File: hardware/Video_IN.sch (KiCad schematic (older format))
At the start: 2 parts, among them U4 DS90CF363AMTD

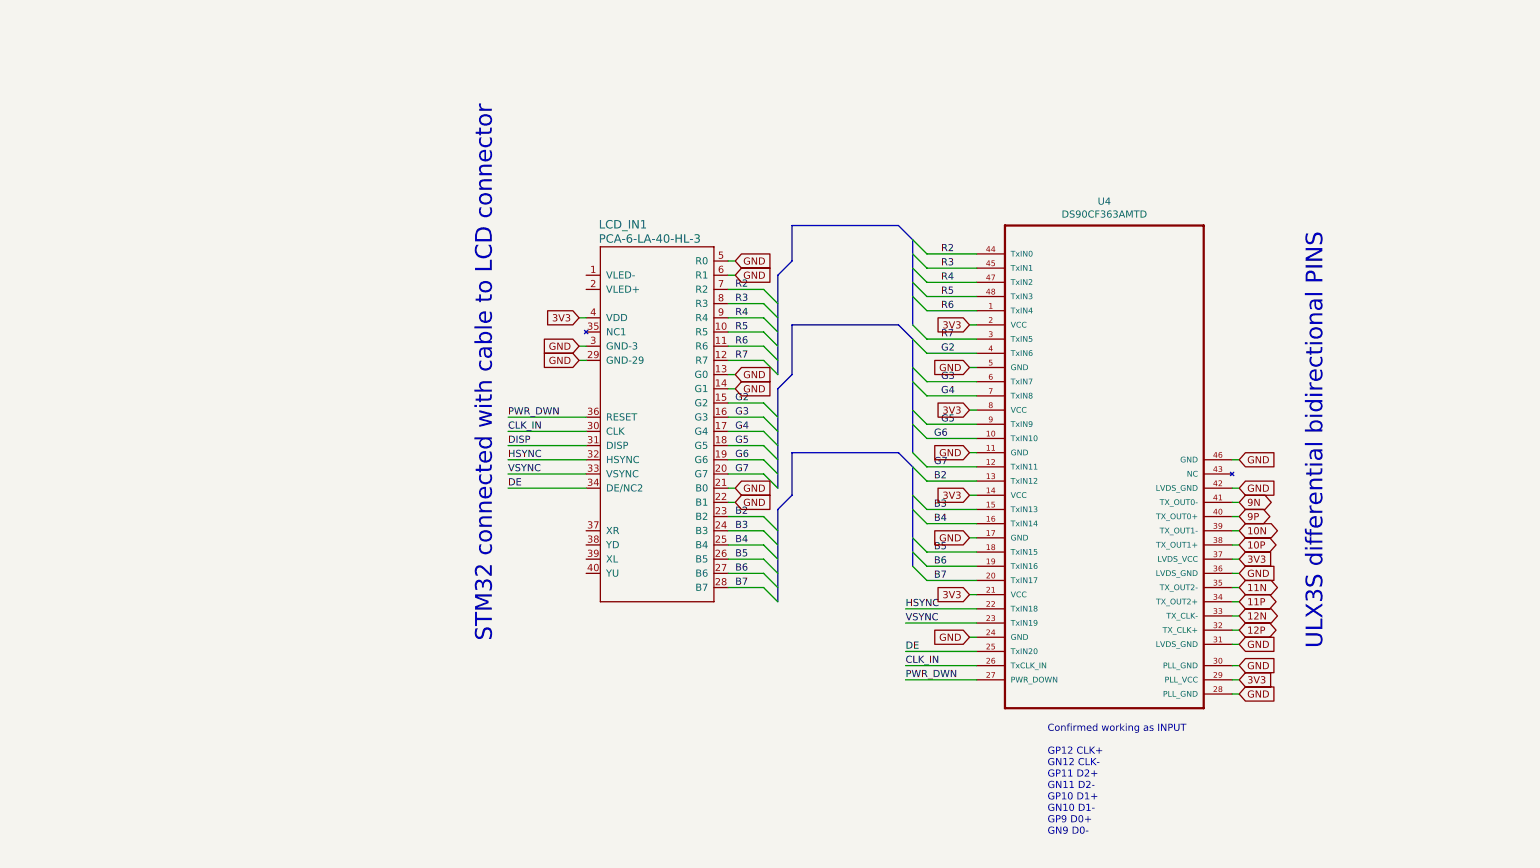
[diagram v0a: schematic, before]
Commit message: Adding decoupling capacitors, termination resoistors for LVDS IN
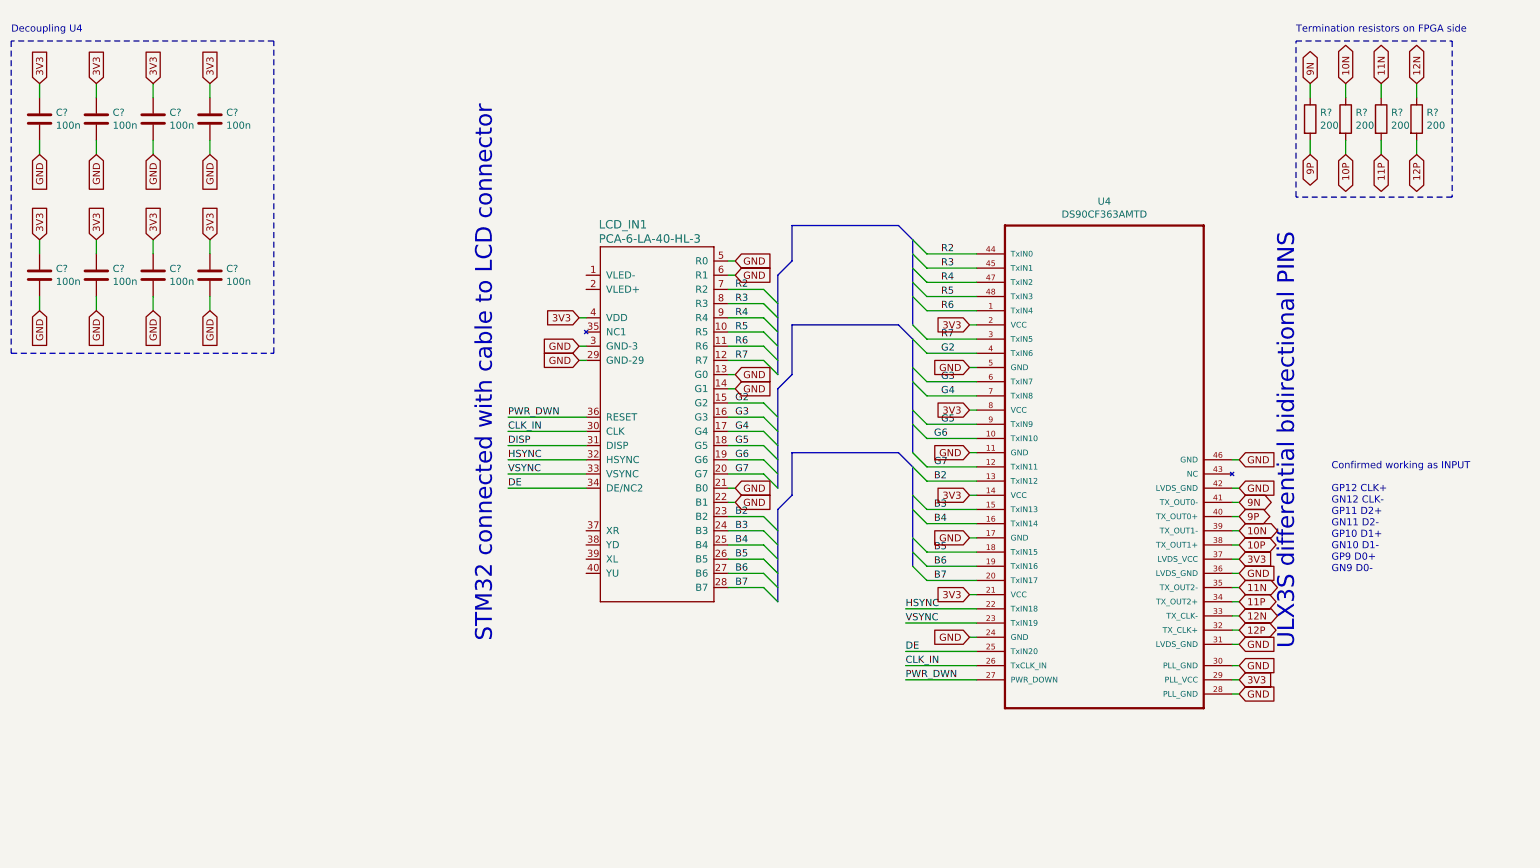
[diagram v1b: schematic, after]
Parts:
- added C? (x8): 100n, symbol antena:C
- added R? (x4): 200, symbol antena:R
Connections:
- net 10N: now also R?.1
- net 10P: now also R?.2
- net 11N: now also R?.1
- net 11P: now also R?.2
- net 12N: now also R?.1
- net 12P: now also R?.2
- net 3V3: now also C?.1, C?.1, C?.1, C?.1, C?.1, C?.1, C?.1, C?.1
- net 9N: now also R?.1
- net 9P: now also R?.2
- net GND: now also C?.2, C?.2, C?.2, C?.2, C?.2, C?.2, C?.2, C?.2
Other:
- note added: "Decoupling U4"
- note added: "Termination resistors on FPGA side"

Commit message: Adding selection resistors
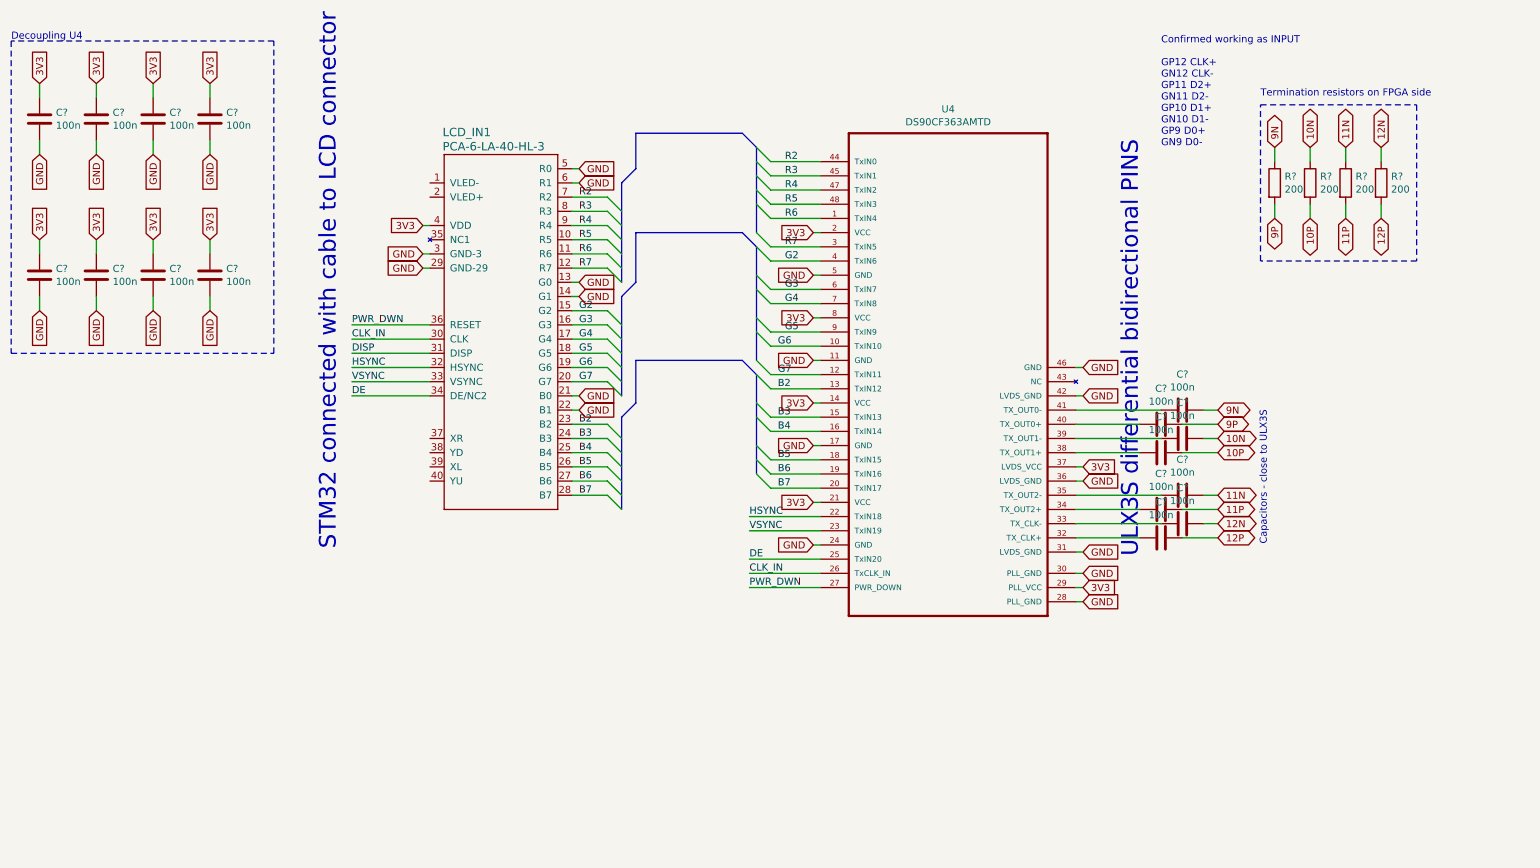
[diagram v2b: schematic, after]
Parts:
- added C? (x8): 100n, symbol antena:C
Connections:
- net 10N: now also C?.1; no longer U4.39 (TX_OUT1-)
- net 10P: now also C?.1; no longer U4.38 (TX_OUT1+)
- net 11N: now also C?.1; no longer U4.35 (TX_OUT2-)
- net 11P: now also C?.1; no longer U4.34 (TX_OUT2+)
- net 12N: now also C?.1; no longer U4.33 (TX_CLK-)
- net 12P: now also C?.1; no longer U4.32 (TX_CLK+)
- net 9N: now also C?.1; no longer U4.41 (TX_OUT0-)
- net 9P: now also C?.1; no longer U4.40 (TX_OUT0+)
- new net: C?.2, U4.32 (TX_CLK+)
- new net: C?.2, U4.33 (TX_CLK-)
- new net: C?.2, U4.34 (TX_OUT2+)
- new net: C?.2, U4.35 (TX_OUT2-)
- new net: C?.2, U4.38 (TX_OUT1+)
- new net: C?.2, U4.39 (TX_OUT1-)
- new net: C?.2, U4.40 (TX_OUT0+)
- new net: C?.2, U4.41 (TX_OUT0-)
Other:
- note added: "Capacitors - close to ULX3S"
- moved on the sheet: LCD_IN1, R?, U4

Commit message: Assigning footprints
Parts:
- C17, C18, C19, C20, C21, C22, C23, C24, C25, C26, C27, C28, C29, C30, C31, C32: renamed from C?; footprint (none) -> Capacitor_SMD:C_0603_1608Metric
- R6, R7, R8, R9: renamed from R?; value 200 -> 100; footprint (none) -> Resistor_SMD:R_0805_2012Metric
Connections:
- net VLED-: now reaches LCD_IN1.1 (VLED-)
- net VLED+: now reaches LCD_IN1.2 (VLED+)
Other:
- moved on the sheet: R6, R7, R8, R9

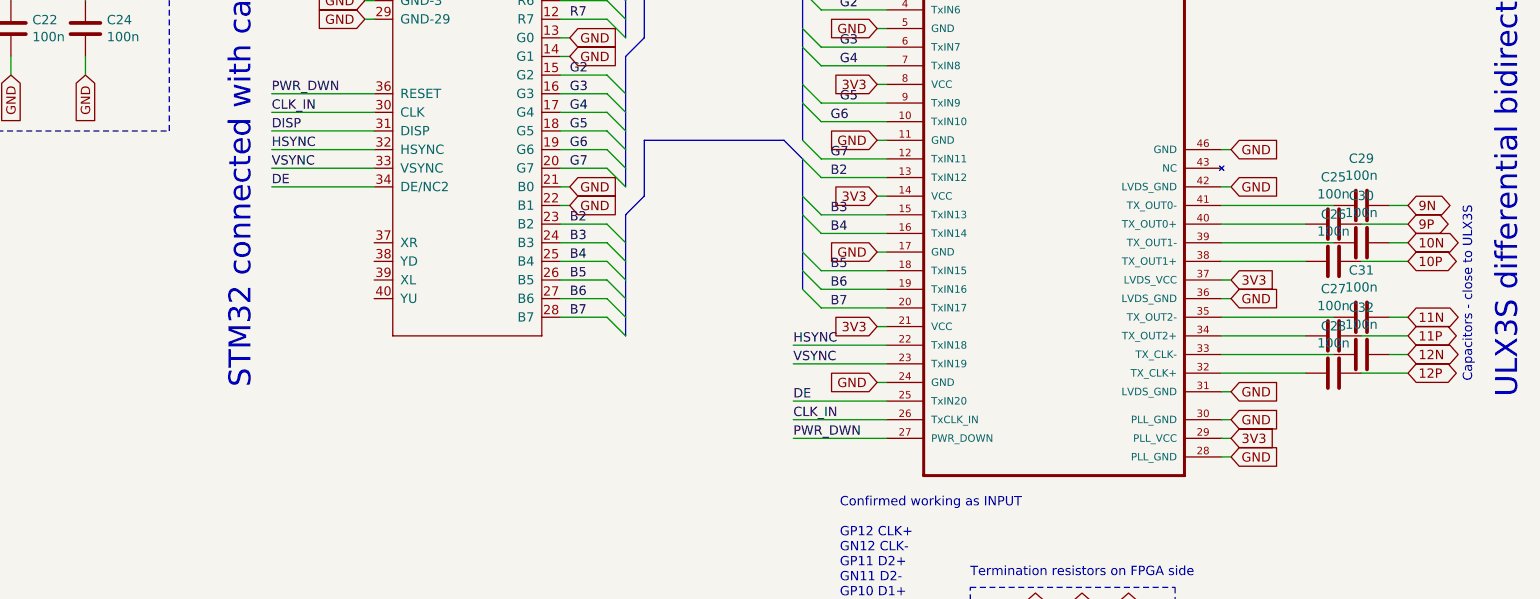
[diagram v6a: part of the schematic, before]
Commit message: Partially connecting ads8586s
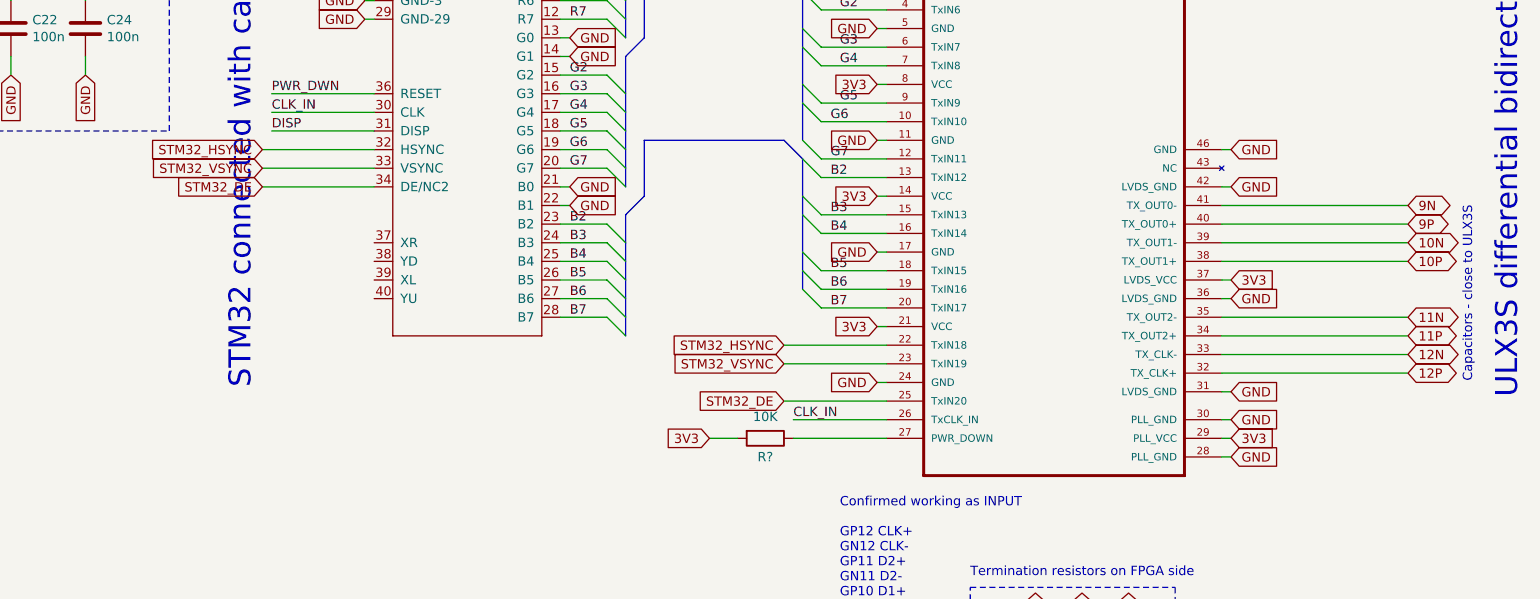
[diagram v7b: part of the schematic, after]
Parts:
- removed C25, C26, C27, C28, C29, C30, C31, C32: 100n, Capacitor_SMD:C_0603_1608Metric, symbol antena:C
- added R?: 10K, symbol antena:R
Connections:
- net 10N: now also U4.39 (TX_OUT1-)
- net 10P: now also U4.38 (TX_OUT1+)
- net 11N: now also U4.35 (TX_OUT2-)
- net 11P: now also U4.34 (TX_OUT2+)
- net 12N: now also U4.33 (TX_CLK-)
- net 12P: now also U4.32 (TX_CLK+)
- net 3V3: now also R?.2
- net 9N: now also U4.41 (TX_OUT0-)
- net 9P: now also U4.40 (TX_OUT0+)
- net PWR_DWN: no longer U4.27 (PWR_DOWN)
- net DE renamed STM32_DE
- net HSYNC renamed STM32_HSYNC
- net VSYNC renamed STM32_VSYNC
- new net: R?.1, U4.27 (PWR_DOWN)
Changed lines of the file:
@@
 Wire Bus Line
 	5100 1400 5850 1400
-Text Label 5900 4100 0    50   ~ 0
-HSYNC
-Text Label 5900 4200 0    50   ~ 0
-VSYNC
-Text Label 5900 4400 0    50   ~ 0
-DE
 Text Label 5900 4500 0    50   ~ 0
 CLK_IN
-Text Label 5900 4600 0    50   ~ 0
-PWR_DWN
-Wire Wire Line
-	5900 4100 6400 4100
-Wire Wire Line
-	5900 4200 6400 4200
-Wire Wire Line
-	5900 4400 6400 4400
 Wire Wire Line
 	5900 4500 6400 4500
@@
 	5900 4600 6400 4600
 Wire Wire Line
-	3650 3050 3100 3050
-Wire Wire Line
-	3650 3150 3100 3150
-Wire Wire Line
-	3650 3250 3100 3250
-Wire Wire Line
 	3650 2850 3100 2850
-Text Label 3100 3050 0    50   ~ 0
-HSYNC
-Text Label 3100 3150 0    50   ~ 0
-VSYNC
-Text Label 3100 3250 0    50   ~ 0
-DE
 Text Label 3100 2850 0    50   ~ 0
 CLK_IN
@@
 Text Notes 6850 5350 0    50   ~ 0
 Termination resistors on FPGA side
-$Comp
-L antena:C C29
-U 1 1 5E54518A
-P 8950 3350
-F 0 "C29" V 8698 3350 50  0000 C CNN
-F 1 "100n" V 8789 3350 50  0000 C CNN
-F 2 "Capacitor_SMD:C_0603_1608Metric" H 8988 3200 50  0001 C CNN
-F 3 "~" H 8950 3350 50  0001 C CNN
-	1    8950 3350
-	0    1    1    0
-$EndComp
-Wire Wire Line
-	9100 3350 9200 3350
-Wire Wire Line
-	8200 3350 8800 3350
-$Comp
-L antena:C C25
-U 1 1 5E54DB8E
-P 8800 3450
-F 0 "C25" V 8548 3450 50  0000 C CNN
-F 1 "100n" V 8639 3450 50  0000 C CNN
-F 2 "Capacitor_SMD:C_0603_1608Metric" H 8838 3300 50  0001 C CNN
-F 3 "~" H 8800 3450 50  0001 C CNN
-	1    8800 3450
-	0    1    1    0
-$EndComp
-$Comp
-L antena:C C30
-U 1 1 5E54DC10
-P 8950 3550
-F 0 "C30" V 8698 3550 50  0000 C CNN
-F 1 "100n" V 8789 3550 50  0000 C CNN
-F 2 "Capacitor_SMD:C_0603_1608Metric" H 8988 3400 50  0001 C CNN
-F 3 "~" H 8950 3550 50  0001 C CNN
-	1    8950 3550
-	0    1    1    0
-$EndComp
-$Comp
-L antena:C C26
-U 1 1 5E54DC4C
-P 8800 3650
-F 0 "C26" V 8548 3650 50  0000 C CNN
-F 1 "100n" V 8639 3650 50  0000 C CNN
-F 2 "Capacitor_SMD:C_0603_1608Metric" H 8838 3500 50  0001 C CNN
-F 3 "~" H 8800 3650 50  0001 C CNN
-	1    8800 3650
-	0    1    1    0
-$EndComp
-$Comp
-L antena:C C31
-U 1 1 5E54DC86
-P 8950 3950
-F 0 "C31" V 8698 3950 50  0000 C CNN
-F 1 "100n" V 8789 3950 50  0000 C CNN
-F 2 "Capacitor_SMD:C_0603_1608Metric" H 8988 3800 50  0001 C CNN
-F 3 "~" H 8950 3950 50  0001 C CNN
-	1    8950 3950
-	0    1    1    0
-$EndComp
-$Comp
-L antena:C C27
-U 1 1 5E54DCEA
-P 8800 4050
-F 0 "C27" V 8548 4050 50  0000 C CNN
-F 1 "100n" V 8639 4050 50  0000 C CNN
-F 2 "Capacitor_SMD:C_0603_1608Metric" H 8838 3900 50  0001 C CNN
-F 3 "~" H 8800 4050 50  0001 C CNN
-	1    8800 4050
-	0    1    1    0
-$EndComp
-$Comp
-L antena:C C32
-U 1 1 5E54DD28
-P 8950 4150
-F 0 "C32" V 8698 4150 50  0000 C CNN
-F 1 "100n" V 8789 4150 50  0000 C CNN
-F 2 "Capacitor_SMD:C_0603_1608Metric" H 8988 4000 50  0001 C CNN
-F 3 "~" H 8950 4150 50  0001 C CNN
-	1    8950 4150
-	0    1    1    0
-$EndComp
-$Comp
-L antena:C C28
-U 1 1 5E54DD6E
-P 8800 4250
-F 0 "C28" V 8548 4250 50  0000 C CNN
-F 1 "100n" V 8639 4250 50  0000 C CNN
-F 2 "Capacitor_SMD:C_0603_1608Metric" H 8838 4100 50  0001 C CNN
-F 3 "~" H 8800 4250 50  0001 C CNN
-	1    8800 4250
-	0    1    1    0
-$EndComp
-Wire Wire Line
-	8950 3450 9200 3450
-Wire Wire Line
-	9100 3550 9200 3550
-Wire Wire Line
-	9200 3650 8950 3650
-Wire Wire Line
-	9100 3950 9200 3950
-Wire Wire Line
-	8950 4050 9200 4050
-Wire Wire Line
-	9200 4150 9100 4150
-Wire Wire Line
-	8950 4250 9200 4250
-Wire Wire Line
-	8200 3450 8650 3450
-Wire Wire Line
-	8200 3550 8800 3550
-Wire Wire Line
-	8200 3650 8650 3650
-Wire Wire Line
-	8200 3950 8800 3950
-Wire Wire Line
-	8200 4050 8650 4050
-Wire Wire Line
-	8200 4150 8800 4150
-Wire Wire Line
-	8200 4250 8650 4250
 Text Notes 9550 4300 1    50   ~ 0
 Capacitors - close to ULX3S
@@
 Wire Wire Line
 	3550 1850 3650 1850
+$Comp
+L antena:R R?
+U 1 1 5E326151
+P 5750 4600
+F 0 "R?" V 5850 4600 50  0000 C CNN
+F 1 "10K" V 5634 4600 50  0000 C CNN
+F 2 "" V 5680 4600 50  0001 C CNN
+F 3 "~" H 5750 4600 50  0001 C CNN
+	1    5750 4600
+	0    1    1    0
+$EndComp
+Text GLabel 5450 4600 0    50   Input ~ 0
+3V3
+Wire Wire Line
+	5450 4600 5600 4600
+Text GLabel 5850 4100 0    50   Input ~ 0
+STM32_HSYNC
+Wire Wire Line
+	5850 4100 6400 4100
+Text GLabel 5850 4200 0    50   Input ~ 0
+STM32_VSYNC
+Wire Wire Line
+	5850 4200 6400 4200
+Text GLabel 5850 4400 0    50   Input ~ 0
+STM32_DE
+Wire Wire Line
+	5850 4400 6400 4400
+Text GLabel 3050 3050 0    50   Input ~ 0
+STM32_HSYNC
+Text GLabel 3050 3150 0    50   Input ~ 0
+STM32_VSYNC
+Text GLabel 3050 3250 0    50   Input ~ 0
+STM32_DE
+Wire Wire Line
+	3050 3050 3650 3050
+Wire Wire Line
+	3050 3150 3650 3150
+Wire Wire Line
+	3050 3250 3650 3250
+Wire Wire Line
+	8200 3350 9200 3350
+Wire Wire Line
+	8200 3450 9200 3450
+Wire Wire Line
+	8200 3550 9200 3550
+Wire Wire Line
+	8200 3650 9200 3650
+Wire Wire Line
+	8200 3950 9200 3950
+Wire Wire Line
+	8200 4050 9200 4050
+Wire Wire Line
+	8200 4150 9200 4150
+Wire Wire Line
+	8200 4250 9200 4250
 Wire Bus Line
 	5950 1500 5950 2100

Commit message: Adding last known changes to shematics
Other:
- note removed: "Capacitors - close to ULX3S"
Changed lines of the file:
@@
 $Descr A4 11693 8268
 encoding utf-8
-Sheet 6 11
+Sheet 6 10
 Title ""
-Date ""
-Rev ""
-Comp ""
+Date "2020-01-29"
+Rev "0.1"
+Comp "Envox d.o.o."
 Comment1 ""
 Comment2 ""
@@
 Text Notes 6150 5700 0    50   ~ 0
 Confirmed working as INPUT\n\nGP12 CLK+\nGN12 CLK-\nGP11 D2+\nGN11 D2-\nGP10 D1+\nGN10 D1-\nGP9 D0+\nGN9 D0-
-Text GLabel 9200 4250 2    50   BiDi ~ 0
+Text GLabel 8250 4250 2    50   BiDi ~ 0
 12P
-Text GLabel 9200 4150 2    50   BiDi ~ 0
+Text GLabel 8250 4150 2    50   BiDi ~ 0
 12N
-Text GLabel 9200 4050 2    50   BiDi ~ 0
+Text GLabel 8250 4050 2    50   BiDi ~ 0
 11P
-Text GLabel 9200 3950 2    50   BiDi ~ 0
+Text GLabel 8250 3950 2    50   BiDi ~ 0
 11N
-Text GLabel 9200 3650 2    50   BiDi ~ 0
+Text GLabel 8250 3650 2    50   BiDi ~ 0
 10P
-Text GLabel 9200 3550 2    50   BiDi ~ 0
+Text GLabel 8250 3550 2    50   BiDi ~ 0
 10N
-Text GLabel 9200 3450 2    50   BiDi ~ 0
+Text GLabel 8250 3450 2    50   BiDi ~ 0
 9P
-Text GLabel 9200 3350 2    50   BiDi ~ 0
+Text GLabel 8250 3350 2    50   BiDi ~ 0
 9N
 Text GLabel 8250 3750 2    50   Input ~ 0
@@
 Text Notes 3000 550  3    118  ~ 0
 STM32 connected with cable to LCD connector
-Text Notes 9800 1450 3    118  ~ 0
+Text Notes 8750 1400 3    118  ~ 0
 ULX3S differential bidirectional PINS
 Text GLabel 900  1050 1    50   Input ~ 0
@@
 Text Notes 6850 5350 0    50   ~ 0
 Termination resistors on FPGA side
-Text Notes 9550 4300 1    50   ~ 0
-Capacitors - close to ULX3S
 Text GLabel 3550 1750 0    50   Input ~ 0
 VLED-
@@
 	3050 3250 3650 3250
 Wire Wire Line
-	8200 3350 9200 3350
-Wire Wire Line
-	8200 3450 9200 3450
-Wire Wire Line
-	8200 3550 9200 3550
-Wire Wire Line
-	8200 3650 9200 3650
-Wire Wire Line
-	8200 3950 9200 3950
-Wire Wire Line
-	8200 4050 9200 4050
-Wire Wire Line
-	8200 4150 9200 4150
-Wire Wire Line
-	8200 4250 9200 4250
+	8200 3350 8250 3350
+Wire Wire Line
+	8200 3450 8250 3450
+Wire Wire Line
+	8200 3550 8250 3550
+Wire Wire Line
+	8200 3650 8250 3650
+Wire Wire Line
+	8200 3950 8250 3950
+Wire Wire Line
+	8200 4050 8250 4050
+Wire Wire Line
+	8200 4150 8250 4150
+Wire Wire Line
+	8200 4250 8250 4250
 Wire Bus Line
 	5950 1500 5950 2100
